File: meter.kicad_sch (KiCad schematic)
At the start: 15 parts, among them SW2 MODE, U2 LM3914N

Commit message: fix: mode switch footprint & silkscreen labels
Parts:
- SW2: footprint Button_Switch_THT:SW_CK_JS202011AQN_DPDT_Angled -> Button_Switch_THT:SW_Slide_SPDT_Angled_CK_OS102011MA1Q
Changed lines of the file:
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@@
 			)
 		)
-		(property "Footprint" "Button_Switch_THT:SW_CK_JS202011AQN_DPDT_Angled"
+		(property "Footprint" "Button_Switch_THT:SW_Slide_SPDT_Angled_CK_OS102011MA1Q"
 			(at 107.95 111.76 0)
 			(effects

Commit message: feat: update with separate freq and period adjustment
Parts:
- R4: value 3.8K -> 3K8
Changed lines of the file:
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@@
 			)
 		)
-		(property "Value" "3.8K"
+		(property "Value" "3K8"
 			(at 52.07 105.41 90)
 			(effects

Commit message: fix: polarised capacitor and erronous silkscreen label
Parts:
- R2: value 1K -> 3K3
- R4: value 3K8 -> 10K
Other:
- note added: "~5V REF 6.25mA drive"
- note removed: "~6V REF 12.5mA drive"
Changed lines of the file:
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@@
 		)
 	)
-	(text "~6V REF\n12.5mA drive"
+	(text "~5V REF\n6.25mA drive"
 		(exclude_from_sim no)
 		(at 29.718 115.824 0)
@@
 			)
 		)
-		(property "Value" "3K8"
+		(property "Value" "10K"
 			(at 52.07 105.41 90)
 			(effects
@@
 			)
 		)
-		(property "Value" "1K"
+		(property "Value" "3K3"
 			(at 52.07 92.71 90)
 			(effects

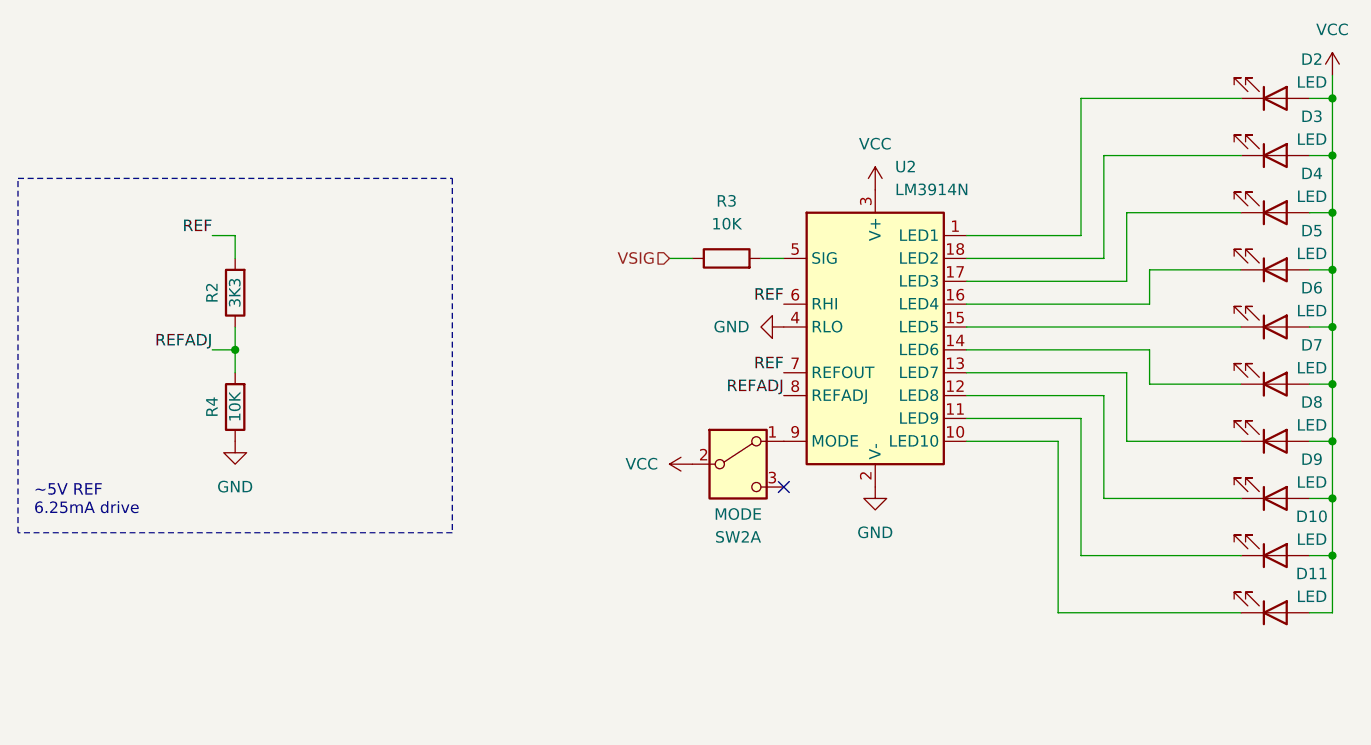
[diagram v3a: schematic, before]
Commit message: feat: refresh majority of pcb to improve ease of assembly
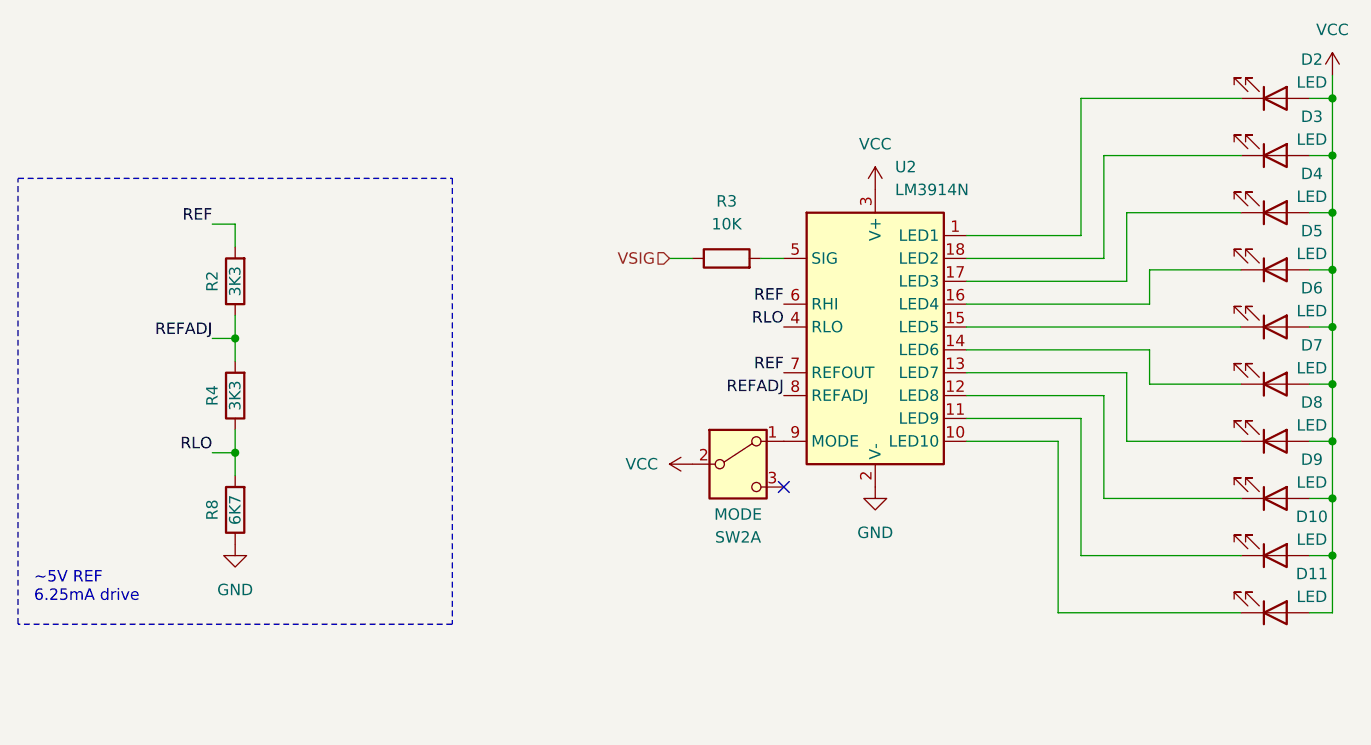
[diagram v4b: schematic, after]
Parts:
- added R8: 6K7, Resistor_THT:R_Axial_DIN0207_L6.3mm_D2.5mm_P7.62mm_Horizontal, symbol Device:R
- R4: value 10K -> 3K3
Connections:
- net GND: now also R8.1; no longer R4.1, U2.4 (RLO)
- new net RLO: R4.1, R8.2, U2.4 (RLO)
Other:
- moved on the sheet: R2, R4
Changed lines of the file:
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@@
+	)
+	(junction
+		(at 52.07 110.49)
+		(diameter 0)
+		(color 0 0 0 0)
 	)
 	(junction
@@
 	)
 	(junction
-		(at 52.07 99.06)
+		(at 52.07 97.79)
 		(diameter 0)
 		(color 0 0 0 0)
@@
 	(wire
 		(pts
-			(xy 52.07 96.52) (xy 52.07 99.06)
+			(xy 52.07 95.25) (xy 52.07 97.79)
 		)
 		(stroke
@@
 	(wire
 		(pts
-			(xy 49.53 99.06) (xy 52.07 99.06)
+			(xy 49.53 97.79) (xy 52.07 97.79)
 		)
 		(stroke
@@
 	(wire
 		(pts
-			(xy 52.07 86.36) (xy 52.07 88.9)
+			(xy 52.07 85.09) (xy 52.07 87.63)
 		)
 		(stroke
@@
 	(wire
 		(pts
+			(xy 52.07 110.49) (xy 52.07 107.95)
+		)
+		(stroke
+			(width 0)
+			(type default)
+		)
+	)
+	(wire
+		(pts
 			(xy 163.83 102.87) (xy 153.67 102.87)
 		)
@@
 	(wire
 		(pts
-			(xy 49.53 86.36) (xy 52.07 86.36)
+			(xy 49.53 85.09) (xy 52.07 85.09)
 		)
 		(stroke
@@
 	(wire
 		(pts
+			(xy 52.07 113.03) (xy 52.07 110.49)
+		)
+		(stroke
+			(width 0)
+			(type default)
+		)
+	)
+	(wire
+		(pts
+			(xy 49.53 110.49) (xy 52.07 110.49)
+		)
+		(stroke
+			(width 0)
+			(type default)
+		)
+	)
+	(wire
+		(pts
 			(xy 151.13 101.6) (xy 151.13 109.22)
 		)
@@
 	(wire
 		(pts
-			(xy 52.07 99.06) (xy 52.07 101.6)
+			(xy 52.07 97.79) (xy 52.07 100.33)
 		)
 		(stroke
@@
 	(rectangle
 		(start 27.94 80.01)
-		(end 76.2 119.38)
+		(end 76.2 129.54)
 		(stroke
 			(width 0)
@@
 	(text "~5V REF\n6.25mA drive"
 		(exclude_from_sim no)
-		(at 29.718 115.824 0)
+		(at 29.718 125.476 0)
 		(effects
 			(font
@@
 		)
 	)
+	(label "RLO"
+		(at 113.03 96.52 180)
+		(fields_autoplaced yes)
+		(effects
+			(font
+				(size 1.27 1.27)
+			)
+			(justify right bottom)
+		)
+	)
+	(label "RLO"
+		(at 49.53 110.49 180)
+		(fields_autoplaced yes)
+		(effects
+			(font
+				(size 1.27 1.27)
+			)
+			(justify right bottom)
+		)
+	)
 	(label "REFADJ"
-		(at 49.53 99.06 180)
+		(at 49.53 97.79 180)
 		(fields_autoplaced yes)
 		(effects
@@
 	)
 	(label "REF"
-		(at 49.53 86.36 180)
+		(at 49.53 85.09 180)
 		(fields_autoplaced yes)
 		(effects
@@
 	)
 	(symbol
-		(lib_id "power:GND")
-		(at 113.03 96.52 270)
-		(unit 1)
-		(exclude_from_sim no)
-		(in_bom yes)
-		(on_board yes)
-		(dnp no)
-		(fields_autoplaced yes)
-		(property "Reference" "#PWR013"
-			(at 106.68 96.52 0)
-			(effects
-				(font
-					(size 1.27 1.27)
-				)
-				(hide yes)
-			)
-		)
-		(property "Value" "GND"
-			(at 109.22 96.5199 90)
-			(effects
-				(font
-					(size 1.27 1.27)
-				)
-				(justify right)
-			)
-		)
-		(property "Footprint" ""
-			(at 113.03 96.52 0)
-			(effects
-				(font
-					(size 1.27 1.27)
-				)
-				(hide yes)
-			)
-		)
-		(property "Datasheet" ""
-			(at 113.03 96.52 0)
-			(effects
-				(font
-					(size 1.27 1.27)
-				)
-				(hide yes)
-			)
-		)
-		(property "Description" "Power symbol creates a global label with name \"GND\" , ground"
-			(at 113.03 96.52 0)
-			(effects
-				(font
-					(size 1.27 1.27)
-				)
-				(hide yes)
-			)
-		)
-		(pin "1"
-		)
-		(instances
-			(project "555Sandbox"
-				(path "/d3ec5529-4071-49eb-a022-408dfaa9f0dc/36bc0783-40fd-4027-87f9-17cbb705ca8e"
-					(reference "#PWR013")
-					(unit 1)
-				)
-			)
-		)
-	)
-	(symbol
 		(lib_id "Device:R")
 		(at 106.68 88.9 90)
@@
 	(symbol
 		(lib_id "Device:R")
-		(at 52.07 105.41 180)
+		(at 52.07 104.14 180)
 		(unit 1)
 		(exclude_from_sim no)
@@
 		(dnp no)
 		(property "Reference" "R4"
-			(at 49.53 105.41 90)
-			(effects
-				(font
-					(size 1.27 1.27)
-				)
-			)
-		)
-		(property "Value" "10K"
-			(at 52.07 105.41 90)
+			(at 49.53 104.14 90)
+			(effects
+				(font
+					(size 1.27 1.27)
+				)
+			)
+		)
+		(property "Value" "3K3"
+			(at 52.07 104.14 90)
 			(effects
 				(font
@@
 		)
 		(property "Footprint" "Resistor_THT:R_Axial_DIN0207_L6.3mm_D2.5mm_P7.62mm_Horizontal"
-			(at 53.848 105.41 90)
+			(at 53.848 104.14 90)
 			(effects
 				(font
@@
 		)
 		(property "Datasheet" "~"
-			(at 52.07 105.41 0)
+			(at 52.07 104.14 0)
 			(effects
 				(font
@@
 		)
 		(property "Description" "Resistor"
-			(at 52.07 105.41 0)
+			(at 52.07 104.14 0)
 			(effects
 				(font
@@
 	(symbol
 		(lib_id "power:GND")
-		(at 52.07 109.22 0)
+		(at 52.07 120.65 0)
 		(unit 1)
 		(exclude_from_sim no)
@@
 		(fields_autoplaced yes)
 		(property "Reference" "#PWR021"
-			(at 52.07 115.57 0)
+			(at 52.07 127 0)
 			(effects
 				(font
@@
 		)
 		(property "Value" "GND"
-			(at 52.07 114.3 0)
+			(at 52.07 125.73 0)
 			(effects
 				(font
@@
 		)
 		(property "Footprint" ""
-			(at 52.07 109.22 0)
+			(at 52.07 120.65 0)
 			(effects
 				(font
@@
 		)
 		(property "Datasheet" ""
-			(at 52.07 109.22 0)
+			(at 52.07 120.65 0)
 			(effects
 				(font
@@
 		)
 		(property "Description" "Power symbol creates a global label with name \"GND\" , ground"
-			(at 52.07 109.22 0)
+			(at 52.07 120.65 0)
 			(effects
 				(font
@@
 	(symbol
 		(lib_id "Device:R")
-		(at 52.07 92.71 180)
+		(at 52.07 116.84 180)
+		(unit 1)
+		(exclude_from_sim no)
+		(in_bom yes)
+		(on_board yes)
+		(dnp no)
+		(property "Reference" "R8"
+			(at 49.53 116.84 90)
+			(effects
+				(font
+					(size 1.27 1.27)
+				)
+			)
+		)
+		(property "Value" "6K7"
+			(at 52.07 116.84 90)
+			(effects
+				(font
+					(size 1.27 1.27)
+				)
+			)
+		)
+		(property "Footprint" "Resistor_THT:R_Axial_DIN0207_L6.3mm_D2.5mm_P7.62mm_Horizontal"
+			(at 53.848 116.84 90)
+			(effects
+				(font
+					(size 1.27 1.27)
+				)
+				(hide yes)
+			)
+		)
+		(property "Datasheet" "~"
+			(at 52.07 116.84 0)
+			(effects
+				(font
+					(size 1.27 1.27)
+				)
+				(hide yes)
+			)
+		)
+		(property "Description" "Resistor"
+			(at 52.07 116.84 0)
+			(effects
+				(font
+					(size 1.27 1.27)
+				)
+				(hide yes)
+			)
+		)
+		(pin "2"
+		)
+		(pin "1"
+		)
+		(instances
+			(project "555Sandbox"
+				(path "/d3ec5529-4071-49eb-a022-408dfaa9f0dc/36bc0783-40fd-4027-87f9-17cbb705ca8e"
+					(reference "R8")
+					(unit 1)
+				)
+			)
+		)
+	)
+	(symbol
+		(lib_id "Device:R")
+		(at 52.07 91.44 180)
 		(unit 1)
 		(exclude_from_sim no)
@@
 		(dnp no)
 		(property "Reference" "R2"
-			(at 49.53 92.71 90)
+			(at 49.53 91.44 90)
 			(effects
 				(font
@@
 		)
 		(property "Value" "3K3"
-			(at 52.07 92.71 90)
+			(at 52.07 91.44 90)
 			(effects
 				(font
@@
 		)
 		(property "Footprint" "Resistor_THT:R_Axial_DIN0207_L6.3mm_D2.5mm_P7.62mm_Horizontal"
-			(at 53.848 92.71 90)
+			(at 53.848 91.44 90)
 			(effects
 				(font
@@
 		)
 		(property "Datasheet" "~"
-			(at 52.07 92.71 0)
+			(at 52.07 91.44 0)
 			(effects
 				(font
@@
 		)
 		(property "Description" "Resistor"
-			(at 52.07 92.71 0)
-			(effects
-				(font
+			(at 52.07 91.44 0)
+			(effects
+				(font

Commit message: patch: split resistor into 2, update silkscreen
allow use of same resistor values instead of an additional 6k7 resistor
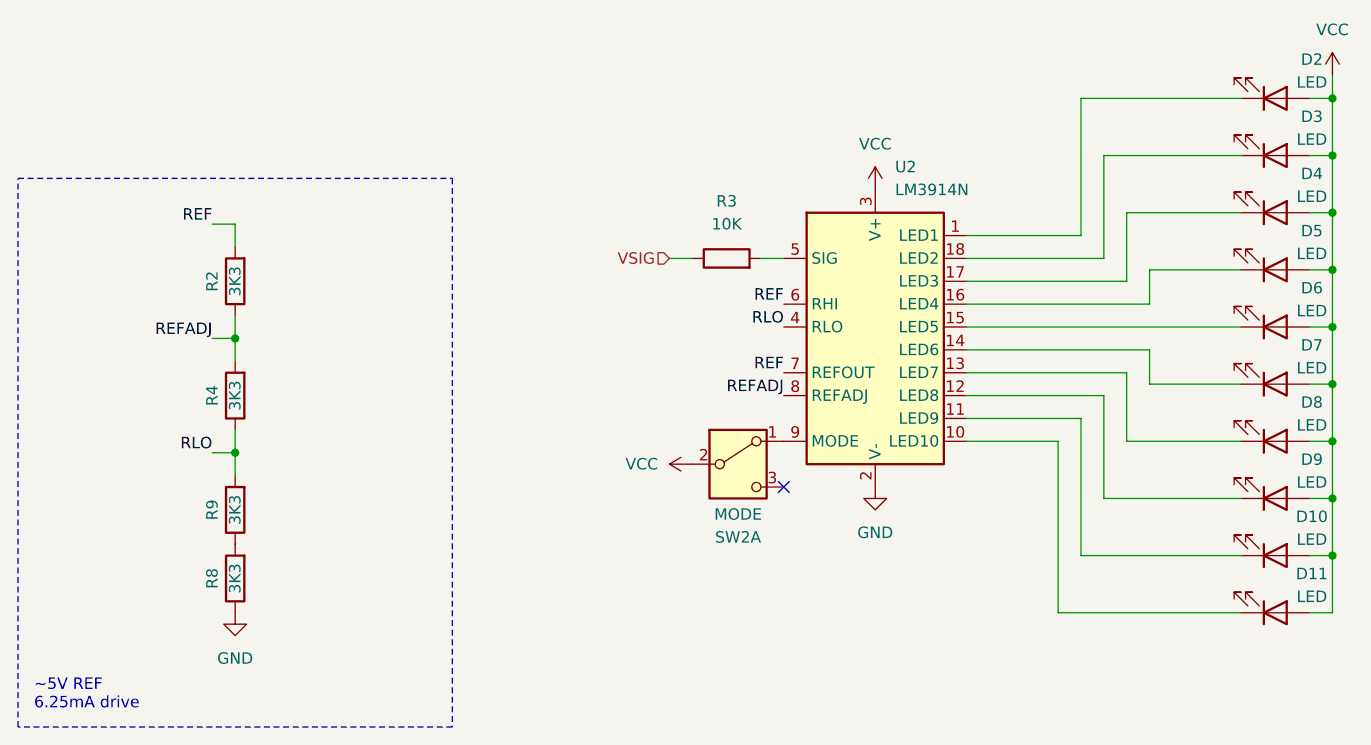
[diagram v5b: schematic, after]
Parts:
- added R9: 3K3, Resistor_THT:R_Axial_DIN0207_L6.3mm_D2.5mm_P2.54mm_Vertical, symbol Device:R
- R8: value 6K7 -> 3K3; footprint Resistor_THT:R_Axial_DIN0207_L6.3mm_D2.5mm_P7.62mm_Horizontal -> Resistor_THT:R_Axial_DIN0207_L6.3mm_D2.5mm_P2.54mm_Vertical
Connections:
- net RLO: now also R9.2; no longer R8.2
- new net: R8.2, R9.1
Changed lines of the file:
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@@
+	)
+	(junction
+		(at 173.99 90.17)
+		(diameter 0)
+		(color 0 0 0 0)
+	)
+	(junction
+		(at 173.99 83.82)
+		(diameter 0)
+		(color 0 0 0 0)
+	)
+	(junction
+		(at 173.99 115.57)
+		(diameter 0)
+		(color 0 0 0 0)
+	)
+	(junction
+		(at 173.99 96.52)
+		(diameter 0)
+		(color 0 0 0 0)
 	)
 	(junction
@@
 	)
 	(junction
-		(at 173.99 90.17)
-		(diameter 0)
-		(color 0 0 0 0)
-	)
-	(junction
-		(at 173.99 83.82)
-		(diameter 0)
-		(color 0 0 0 0)
-	)
-	(junction
-		(at 173.99 115.57)
-		(diameter 0)
-		(color 0 0 0 0)
-	)
-	(junction
-		(at 173.99 96.52)
-		(diameter 0)
-		(color 0 0 0 0)
-	)
-	(junction
 		(at 52.07 97.79)
 		(diameter 0)
@@
 	(wire
 		(pts
+			(xy 52.07 110.49) (xy 52.07 113.03)
+		)
+		(stroke
+			(width 0)
+			(type default)
+		)
+	)
+	(wire
+		(pts
 			(xy 171.45 77.47) (xy 173.99 77.47)
 		)
@@
 		(pts
 			(xy 163.83 90.17) (xy 153.67 90.17)
-		)
-		(stroke
-			(width 0)
-			(type default)
-		)
-	)
-	(wire
-		(pts
-			(xy 52.07 113.03) (xy 52.07 110.49)
 		)
 		(stroke
@@
 	(rectangle
 		(start 27.94 80.01)
-		(end 76.2 129.54)
+		(end 76.2 140.97)
 		(stroke
 			(width 0)
@@
 	(text "~5V REF\n6.25mA drive"
 		(exclude_from_sim no)
-		(at 29.718 125.476 0)
+		(at 29.718 137.414 0)
 		(effects
 			(font
@@
 	)
 	(symbol
+		(lib_id "Device:R")
+		(at 52.07 124.46 180)
+		(unit 1)
+		(exclude_from_sim no)
+		(in_bom yes)
+		(on_board yes)
+		(dnp no)
+		(property "Reference" "R8"
+			(at 49.53 124.46 90)
+			(effects
+				(font
+					(size 1.27 1.27)
+				)
+			)
+		)
+		(property "Value" "3K3"
+			(at 52.07 124.46 90)
+			(effects
+				(font
+					(size 1.27 1.27)
+				)
+			)
+		)
+		(property "Footprint" "Resistor_THT:R_Axial_DIN0207_L6.3mm_D2.5mm_P2.54mm_Vertical"
+			(at 53.848 124.46 90)
+			(effects
+				(font
+					(size 1.27 1.27)
+				)
+				(hide yes)
+			)
+		)
+		(property "Datasheet" "~"
+			(at 52.07 124.46 0)
+			(effects
+				(font
+					(size 1.27 1.27)
+				)
+				(hide yes)
+			)
+		)
+		(property "Description" "Resistor"
+			(at 52.07 124.46 0)
+			(effects
+				(font
+					(size 1.27 1.27)
+				)
+				(hide yes)
+			)
+		)
+		(pin "2"
+		)
+		(pin "1"
+		)
+		(instances
+			(project "555Sandbox"
+				(path "/d3ec5529-4071-49eb-a022-408dfaa9f0dc/36bc0783-40fd-4027-87f9-17cbb705ca8e"
+					(reference "R8")
+					(unit 1)
+				)
+			)
+		)
+	)
+	(symbol
 		(lib_id "Device:LED")
 		(at 167.64 77.47 0)
@@
 	(symbol
 		(lib_id "power:GND")
-		(at 52.07 120.65 0)
+		(at 52.07 128.27 0)
 		(unit 1)
 		(exclude_from_sim no)
@@
 		(fields_autoplaced yes)
 		(property "Reference" "#PWR021"
-			(at 52.07 127 0)
+			(at 52.07 134.62 0)
 			(effects
 				(font
@@
 		)
 		(property "Value" "GND"
-			(at 52.07 125.73 0)
+			(at 52.07 133.35 0)
 			(effects
 				(font
@@
 		)
 		(property "Footprint" ""
-			(at 52.07 120.65 0)
+			(at 52.07 128.27 0)
 			(effects
 				(font
@@
 		)
 		(property "Datasheet" ""
-			(at 52.07 120.65 0)
+			(at 52.07 128.27 0)
 			(effects
 				(font
@@
 		)
 		(property "Description" "Power symbol creates a global label with name \"GND\" , ground"
-			(at 52.07 120.65 0)
+			(at 52.07 128.27 0)
 			(effects
 				(font
@@
 				(path "/d3ec5529-4071-49eb-a022-408dfaa9f0dc/36bc0783-40fd-4027-87f9-17cbb705ca8e"
 					(reference "#PWR021")
+					(unit 1)
+				)
+			)
+		)
+	)
+	(symbol
+		(lib_id "Device:R")
+		(at 52.07 116.84 180)
+		(unit 1)
+		(exclude_from_sim no)
+		(in_bom yes)
+		(on_board yes)
+		(dnp no)
+		(property "Reference" "R9"
+			(at 49.53 116.84 90)
+			(effects
+				(font
+					(size 1.27 1.27)
+				)
+			)
+		)
+		(property "Value" "3K3"
+			(at 52.07 116.84 90)
+			(effects
+				(font
+					(size 1.27 1.27)
+				)
+			)
+		)
+		(property "Footprint" "Resistor_THT:R_Axial_DIN0207_L6.3mm_D2.5mm_P2.54mm_Vertical"
+			(at 53.848 116.84 90)
+			(effects
+				(font
+					(size 1.27 1.27)
+				)
+				(hide yes)
+			)
+		)
+		(property "Datasheet" "~"
+			(at 52.07 116.84 0)
+			(effects
+				(font
+					(size 1.27 1.27)
+				)
+				(hide yes)
+			)
+		)
+		(property "Description" "Resistor"
+			(at 52.07 116.84 0)
+			(effects
+				(font
+					(size 1.27 1.27)
+				)
+				(hide yes)
+			)
+		)
+		(pin "2"
+		)
+		(pin "1"
+		)
+		(instances
+			(project "555Sandbox"
+				(path "/d3ec5529-4071-49eb-a022-408dfaa9f0dc/36bc0783-40fd-4027-87f9-17cbb705ca8e"
+					(reference "R9")
 					(unit 1)
 				)
@@
 					(unit 1)
 				)
-			)
-		)
-	)
-	(symbol
-		(lib_id "Device:R")
-		(at 52.07 116.84 180)
-		(unit 1)
-		(exclude_from_sim no)
-		(in_bom yes)
-		(on_board yes)
-		(dnp no)
-		(property "Reference" "R8"
-			(at 49.53 116.84 90)
-			(effects
-				(font
-					(size 1.27 1.27)
-				)
-			)
-		)
-		(property "Value" "6K7"
-			(at 52.07 116.84 90)
-			(effects
-				(font
-					(size 1.27 1.27)
-				)
-			)
-		)
-		(property "Footprint" "Resistor_THT:R_Axial_DIN0207_L6.3mm_D2.5mm_P7.62mm_Horizontal"
-			(at 53.848 116.84 90)
-			(effects
-				(font
-					(size 1.27 1.27)
-				)
-				(hide yes)
-			)
-		)
-		(property "Datasheet" "~"
-			(at 52.07 116.84 0)
-			(effects
-				(font
-					(size 1.27 1.27)
-				)
-				(hide yes)
-			)
-		)
-		(property "Description" "Resistor"
-			(at 52.07 116.84 0)
-			(effects
-				(font
-					(size 1.27 1.27)
-				)
-				(hide yes)
-			)
-		)
-		(pin "2"
-		)
-		(pin "1"
-		)
-		(instances
-			(project "555Sandbox"
-				(path "/d3ec5529-4071-49eb-a022-408dfaa9f0dc/36bc0783-40fd-4027-87f9-17cbb705ca8e"
-					(reference "R8")
-					(unit 1)
-				)

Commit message: feat: board v1.4
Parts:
- R8, R9: value 3K3 -> 2K
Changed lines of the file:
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@@
 			)
 		)
-		(property "Value" "3K3"
+		(property "Value" "2K"
 			(at 52.07 124.46 90)
 			(effects
@@
 			)
 		)
-		(property "Value" "3K3"
+		(property "Value" "2K"
 			(at 52.07 116.84 90)
 			(effects
